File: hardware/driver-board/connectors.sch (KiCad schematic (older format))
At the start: 1 part, among them J1 Conn_01x11_Male

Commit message: Rework power to four different voltage domains
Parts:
- removed J1: Conn_01x11_Male, Connector_PinSocket_2.54mm:PinSocket_1x11_P2.54mm_Vertical, symbol Connector:Conn_01x11_Male
- added J1: Conn_01x10_Male, Connector_PinHeader_2.54mm:PinHeader_1x10_P2.54mm_Vertical, symbol Connector:Conn_01x10_Male
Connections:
- net labels added: VCC
- net labels removed: 12V, GND12V
- wire segments 11 -> 0
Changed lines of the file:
@@
 $EndDescr
 $Comp
-L Connector:Conn_01x11_Male J1
-U 1 1 5EFE0C5D
-P 5400 3850
-F 0 "J1" H 5400 4450 50  0000 C CNN
-F 1 "Conn_01x11_Male" H 5508 4440 50  0001 C CNN
-F 2 "Connector_PinSocket_2.54mm:PinSocket_1x11_P2.54mm_Vertical" H 5400 3850 50  0001 C CNN
-F 3 "~" H 5400 3850 50  0001 C CNN
-	1    5400 3850
+L Connector:Conn_01x10_Male J1
+U 1 1 5F0472A1
+P 5450 3800
+F 0 "J1" H 5558 4289 50  0000 C CNN
+F 1 "Conn_01x10_Male" H 5558 4290 50  0001 C CNN
+F 2 "Connector_PinHeader_2.54mm:PinHeader_1x10_P2.54mm_Vertical" H 5450 3800 50  0001 C CNN
+F 3 "~" H 5450 3800 50  0001 C CNN
+	1    5450 3800
 	1    0    0    -1
 $EndComp
-Wire Wire Line
-	5600 3350 5850 3350
-Wire Wire Line
-	5600 3450 5850 3450
-Wire Wire Line
-	5600 3550 5850 3550
-Wire Wire Line
-	5600 3650 5850 3650
-Wire Wire Line
-	5600 3750 5850 3750
-Wire Wire Line
-	5600 3850 5850 3850
-Wire Wire Line
-	5600 3950 5850 3950
-Wire Wire Line
-	5600 4050 5850 4050
-Wire Wire Line
-	5600 4150 5850 4150
-Wire Wire Line
-	5600 4250 5850 4250
-Wire Wire Line
-	5600 4350 5850 4350
-Text GLabel 5850 4350 2    50   Input ~ 0
-AUDIO
-Text GLabel 5850 4250 2    50   Output ~ 0
-DC
-Text GLabel 5850 4150 2    50   Output ~ 0
-CS2
-Text GLabel 5850 4050 2    50   Output ~ 0
-CS1
-Text GLabel 5850 3950 2    50   Output ~ 0
-MOSI
-Text GLabel 5850 3850 2    50   Input ~ 0
-MISO
-Text GLabel 5850 3750 2    50   Output ~ 0
-CLK
 $Comp
-L power:GND #PWR015
-U 1 1 5EFF5A7A
-P 5850 3650
-F 0 "#PWR015" H 5850 3400 50  0001 C CNN
-F 1 "GND" V 5850 3550 50  0000 R CNN
-F 2 "" H 5850 3650 50  0001 C CNN
-F 3 "" H 5850 3650 50  0001 C CNN
-	1    5850 3650
+L power:+5V #PWR026
+U 1 1 5F04918A
+P 5650 3400
+F 0 "#PWR026" H 5650 3250 50  0001 C CNN
+F 1 "+5V" V 5650 3500 50  0000 L CNN
+F 2 "" H 5650 3400 50  0001 C CNN
+F 3 "" H 5650 3400 50  0001 C CNN
+	1    5650 3400
+	0    1    1    0
+$EndComp
+$Comp
+L power:VCC #PWR027
+U 1 1 5F0493A4
+P 5650 3500
+F 0 "#PWR027" H 5650 3350 50  0001 C CNN
+F 1 "VCC" V 5650 3600 50  0000 L CNN
+F 2 "" H 5650 3500 50  0001 C CNN
+F 3 "" H 5650 3500 50  0001 C CNN
+	1    5650 3500
+	0    1    1    0
+$EndComp
+$Comp
+L power:GND #PWR028
+U 1 1 5F04A2D5
+P 5650 3600
+F 0 "#PWR028" H 5650 3350 50  0001 C CNN
+F 1 "GND" V 5650 3500 50  0000 R CNN
+F 2 "" H 5650 3600 50  0001 C CNN
+F 3 "" H 5650 3600 50  0001 C CNN
+	1    5650 3600
 	0    -1   -1   0
 $EndComp
-$Comp
-L power:+5V #PWR014
-U 1 1 5EFF5C1B
-P 5850 3550
-F 0 "#PWR014" H 5850 3400 50  0001 C CNN
-F 1 "+5V" V 5850 3650 50  0000 L CNN
-F 2 "" H 5850 3550 50  0001 C CNN
-F 3 "" H 5850 3550 50  0001 C CNN
-	1    5850 3550
-	0    1    1    0
-$EndComp
-Text GLabel 5850 3450 2    50   Output ~ 0
-GND12V
-Text GLabel 5850 3350 2    50   Output ~ 0
-12V
+Text GLabel 5650 3700 2    50   Output ~ 0
+CLK
+Text GLabel 5650 3800 2    50   Input ~ 0
+MISO
+Text GLabel 5650 3900 2    50   Output ~ 0
+MOSI
+Text GLabel 5650 4000 2    50   Output ~ 0
+CS1
+Text GLabel 5650 4100 2    50   Output ~ 0
+CS2
+Text GLabel 5650 4200 2    50   Output ~ 0
+DC
+Text GLabel 5650 4300 2    50   Input ~ 0
+AUDIO
 $EndSCHEMATC

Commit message: Add display schematics
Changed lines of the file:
@@
 $Descr A4 11693 8268
 encoding utf-8
-Sheet 4 6
+Sheet 4 7
 Title "FT81x TFT040 Driver Board"
-Date "2020-07-03"
+Date "2020-07-05"
 Rev "2007D"
 Comp ""
@@
 U 1 1 5F0472A1
 P 5450 3800
-F 0 "J1" H 5558 4289 50  0000 C CNN
+F 0 "J1" H 5350 3800 50  0000 C CNN
 F 1 "Conn_01x10_Male" H 5558 4290 50  0001 C CNN
 F 2 "Connector_PinHeader_2.54mm:PinHeader_1x10_P2.54mm_Vertical" H 5450 3800 50  0001 C CNN
@@
 	1    5450 3800
 	1    0    0    -1
-$EndComp
-$Comp
-L power:+5V #PWR026
-U 1 1 5F04918A
-P 5650 3400
-F 0 "#PWR026" H 5650 3250 50  0001 C CNN
-F 1 "+5V" V 5650 3500 50  0000 L CNN
-F 2 "" H 5650 3400 50  0001 C CNN
-F 3 "" H 5650 3400 50  0001 C CNN
-	1    5650 3400
-	0    1    1    0
-$EndComp
-$Comp
-L power:VCC #PWR027
-U 1 1 5F0493A4
-P 5650 3500
-F 0 "#PWR027" H 5650 3350 50  0001 C CNN
-F 1 "VCC" V 5650 3600 50  0000 L CNN
-F 2 "" H 5650 3500 50  0001 C CNN
-F 3 "" H 5650 3500 50  0001 C CNN
-	1    5650 3500
-	0    1    1    0
-$EndComp
-$Comp
-L power:GND #PWR028
-U 1 1 5F04A2D5
-P 5650 3600
-F 0 "#PWR028" H 5650 3350 50  0001 C CNN
-F 1 "GND" V 5650 3500 50  0000 R CNN
-F 2 "" H 5650 3600 50  0001 C CNN
-F 3 "" H 5650 3600 50  0001 C CNN
-	1    5650 3600
-	0    -1   -1   0
 $EndComp
 Text GLabel 5650 3700 2    50   Output ~ 0
@@
 Text GLabel 5650 4300 2    50   Input ~ 0
 AUDIO
+Wire Wire Line
+	5650 3600 6350 3600
+Wire Wire Line
+	5650 3500 6000 3500
+$Comp
+L power:PWR_FLAG #FLG03
+U 1 1 5F08BC00
+P 6350 3600
+F 0 "#FLG03" H 6350 3675 50  0001 C CNN
+F 1 "PWR_FLAG" H 6350 3773 50  0001 C CNN
+F 2 "" H 6350 3600 50  0001 C CNN
+F 3 "~" H 6350 3600 50  0001 C CNN
+	1    6350 3600
+	1    0    0    -1
+$EndComp
+$Comp
+L power:PWR_FLAG #FLG02
+U 1 1 5F08C692
+P 6000 3500
+F 0 "#FLG02" H 6000 3575 50  0001 C CNN
+F 1 "PWR_FLAG" H 6000 3673 50  0001 C CNN
+F 2 "" H 6000 3500 50  0001 C CNN
+F 3 "~" H 6000 3500 50  0001 C CNN
+	1    6000 3500
+	1    0    0    -1
+$EndComp
+$Comp
+L power:PWR_FLAG #FLG01
+U 1 1 5F08C772
+P 5650 3400
+F 0 "#FLG01" H 5650 3475 50  0001 C CNN
+F 1 "PWR_FLAG" H 5650 3573 50  0001 C CNN
+F 2 "" H 5650 3400 50  0001 C CNN
+F 3 "~" H 5650 3400 50  0001 C CNN
+	1    5650 3400
+	1    0    0    -1
+$EndComp
+$Comp
+L power:VCC #PWR027
+U 1 1 5F08CAB0
+P 6000 3500
+F 0 "#PWR027" H 6000 3350 50  0001 C CNN
+F 1 "VCC" V 6000 3600 50  0000 L CNN
+F 2 "" H 6000 3500 50  0001 C CNN
+F 3 "" H 6000 3500 50  0001 C CNN
+	1    6000 3500
+	0    1    1    0
+$EndComp
+Connection ~ 6000 3500
+$Comp
+L power:+5V #PWR026
+U 1 1 5F08CC55
+P 5650 3400
+F 0 "#PWR026" H 5650 3250 50  0001 C CNN
+F 1 "+5V" V 5650 3500 50  0000 L CNN
+F 2 "" H 5650 3400 50  0001 C CNN
+F 3 "" H 5650 3400 50  0001 C CNN
+	1    5650 3400
+	0    1    1    0
+$EndComp
+Connection ~ 5650 3400
+$Comp
+L power:GND #PWR028
+U 1 1 5F091C1E
+P 6350 3600
+F 0 "#PWR028" H 6350 3350 50  0001 C CNN
+F 1 "GND" H 6350 3450 50  0000 C CNN
+F 2 "" H 6350 3600 50  0001 C CNN
+F 3 "" H 6350 3600 50  0001 C CNN
+	1    6350 3600
+	1    0    0    -1
+$EndComp
+Connection ~ 6350 3600
 $EndSCHEMATC

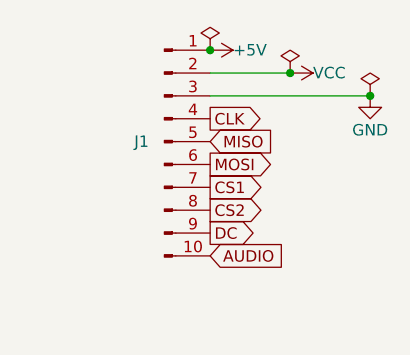
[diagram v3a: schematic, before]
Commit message: Add more pin header pins
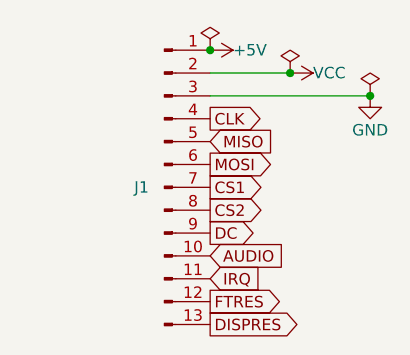
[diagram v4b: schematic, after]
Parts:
- removed J1: Conn_01x10_Male, Connector_PinHeader_2.54mm:PinHeader_1x10_P2.54mm_Vertical, symbol Connector:Conn_01x10_Male
- added J1: Conn_01x13_Male, Connector_PinHeader_2.54mm:PinHeader_1x13_P2.54mm_Vertical, symbol Connector:Conn_01x13_Male
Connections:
- net +5V: now also J1.1 (Pin_1)
- net AUDIO: now also J1.10 (Pin_10)
- net CLK: now also J1.4 (Pin_4)
- net CS1: now also J1.7 (Pin_7)
- net CS2: now also J1.8 (Pin_8)
- net DC: now also J1.9 (Pin_9)
- net GND: now also J1.3 (Pin_3)
- net MISO: now also J1.5 (Pin_5)
- net MOSI: now also J1.6 (Pin_6)
- net VCC: now also J1.2 (Pin_2)
- new net DISPRES: J1.13 (Pin_13)
- new net FTRES: J1.12 (Pin_12)
- new net IRQ: J1.11 (Pin_11)
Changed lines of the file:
@@
 Comment4 ""
 $EndDescr
-$Comp
-L Connector:Conn_01x10_Male J1
-U 1 1 5F0472A1
-P 5450 3800
-F 0 "J1" H 5350 3800 50  0000 C CNN
-F 1 "Conn_01x10_Male" H 5558 4290 50  0001 C CNN
-F 2 "Connector_PinHeader_2.54mm:PinHeader_1x10_P2.54mm_Vertical" H 5450 3800 50  0001 C CNN
-F 3 "~" H 5450 3800 50  0001 C CNN
-	1    5450 3800
-	1    0    0    -1
-$EndComp
 Text GLabel 5650 3700 2    50   Output ~ 0
 CLK
@@
 	0    1    1    0
 $EndComp
-Connection ~ 5650 3400
 $Comp
 L power:GND #PWR028
@@
 $EndComp
 Connection ~ 6350 3600
+$Comp
+L Connector:Conn_01x13_Male J1
+U 1 1 5F05D8EE
+P 5450 4000
+F 0 "J1" H 5350 4000 50  0000 C CNN
+F 1 "Conn_01x13_Male" H 5558 4690 50  0001 C CNN
+F 2 "Connector_PinHeader_2.54mm:PinHeader_1x13_P2.54mm_Vertical" H 5450 4000 50  0001 C CNN
+F 3 "~" H 5450 4000 50  0001 C CNN
+	1    5450 4000
+	1    0    0    -1
+$EndComp
+Connection ~ 5650 3400
+Text GLabel 5650 4400 2    50   Input ~ 0
+IRQ
+Text GLabel 5650 4500 2    50   Output ~ 0
+FTRES
+Text GLabel 5650 4600 2    50   Output ~ 0
+DISPRES
 $EndSCHEMATC

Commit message: Adapt new SPI signal names from OSHWA
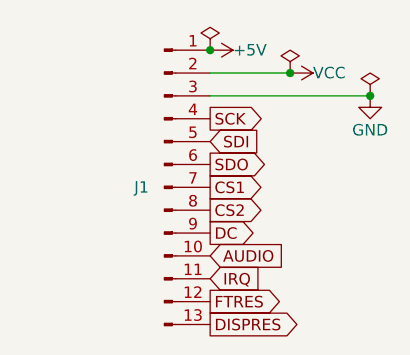
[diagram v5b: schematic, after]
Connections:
- net CLK renamed SCK
- net MISO renamed SDI
- net MOSI renamed SDO
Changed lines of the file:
@@
 $EndDescr
 Text GLabel 5650 3700 2    50   Output ~ 0
-CLK
+SCK
 Text GLabel 5650 3800 2    50   Input ~ 0
-MISO
+SDI
 Text GLabel 5650 3900 2    50   Output ~ 0
-MOSI
+SDO
 Text GLabel 5650 4000 2    50   Output ~ 0
 CS1
